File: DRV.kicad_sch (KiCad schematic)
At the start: 51 parts, among them J2 01x03_MotorTerminal, Q1 NE006NG, Q2 NE006NG, Q3 NE006NG, Q4 NE006NG, Q5 NE006NG, Q6 NE006NG, U7 DRV8353SRTAR

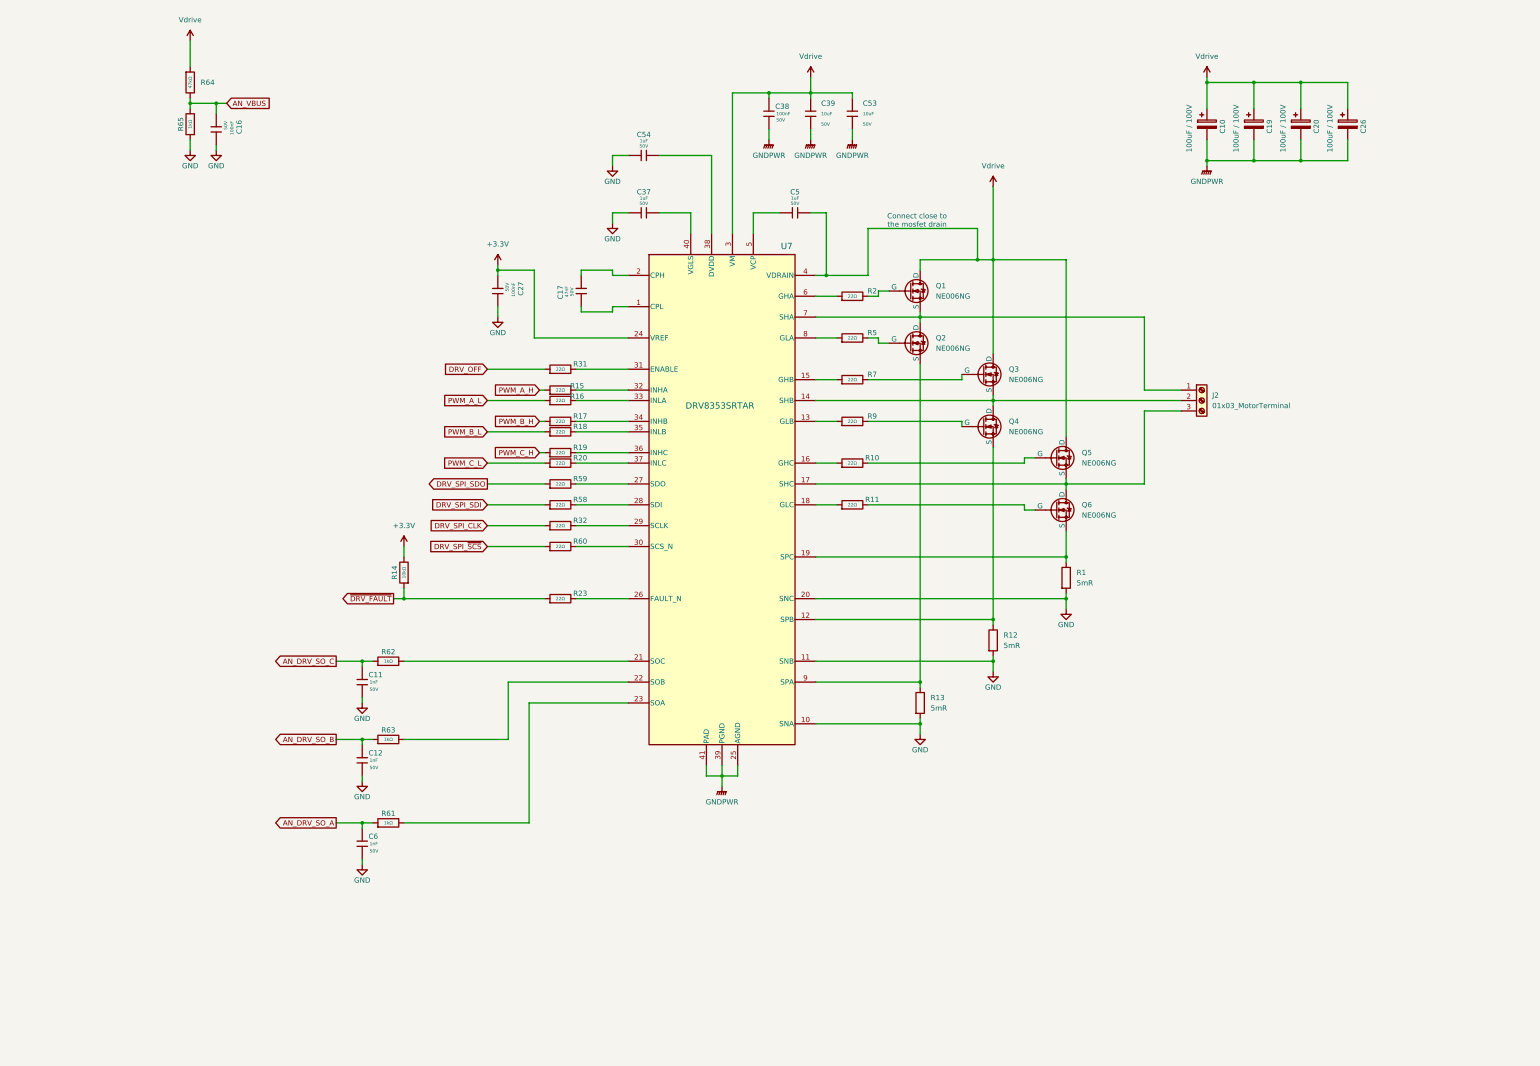
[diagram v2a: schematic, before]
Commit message: Circular pcb edge cut
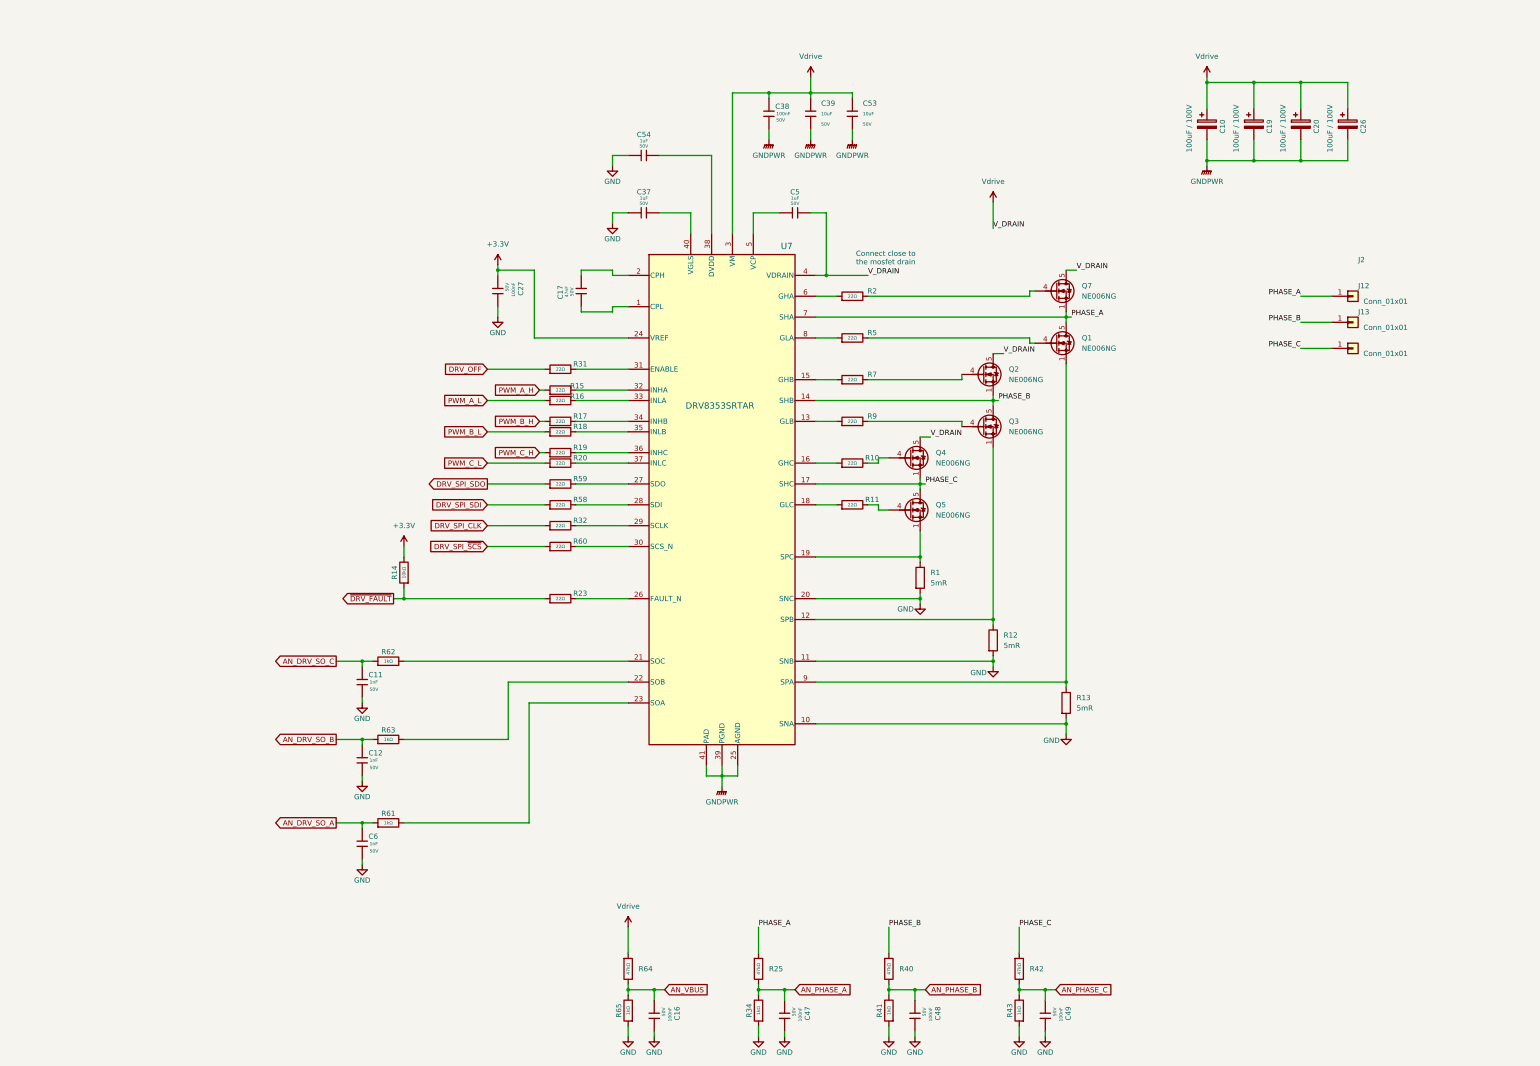
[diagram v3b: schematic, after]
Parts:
- removed J2: 01x03_MotorTerminal, Connector_Phoenix_MC:PhoenixContact_MC_1,5_3-G-3.5_1x03_P3.50mm_Horizontal, symbol Connector:Screw_Terminal_01x03
- removed Q1, Q2, Q3, Q4, Q5, Q6: NE006NG, Package_DFN_QFN:AO_DFN-8-1EP_5.55x5.2mm_P1.27mm_EP4.12x4.6mm, symbol Simulation_SPICE:NMOS
- added C47, C48, C49: 100nF, PCM_JLCPCB:C_0603, symbol PCM_JLCPCB-Capacitors:0603,100nF
- added J12, J13, J2: Conn_01x01, Connector_Wire:SolderWire-2.5sqmm_1x01_D2.4mm_OD3.6mm, symbol Connector_Generic:Conn_01x01
- added Q1, Q2, Q3, Q4, Q5, Q7: NE006NG, Package_DFN_QFN:AO_DFN-8-1EP_5.55x5.2mm_P1.27mm_EP4.12x4.6mm, symbol Transistor_FET:FDMS8350LET40
- added R25, R40, R42: 47kΩ, PCM_JLCPCB:R_0603, symbol PCM_JLCPCB-Resistors:0603,47kΩ
- added R34, R41, R43: 1kΩ, PCM_JLCPCB:R_0603, symbol PCM_JLCPCB-Resistors:0603,1kΩ
- U7: footprint RTA0040B -> footprints:RTA0040B
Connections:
- net GND: now also C47.2, C48.2, C49.2, R34.1, R41.1, R43.1
- net Vdrive: now also Q2.5 (D), Q4.5 (D), Q7.5 (D)
- net at R10.2: now also Q4.4 (G)
- net PHASE_C: now reaches U7.17 (SHC)
- net PHASE_C: now also J13.1 (Pin_1), Q4.1 (S), Q4.2 (S), Q4.3 (S), Q5.5 (D), R42.1
- net at R5.2: now also Q1.4 (G)
- net at R13.1, U7.9 (SPA): now also Q1.1 (S), Q1.2 (S), Q1.3 (S)
- net PHASE_A: now reaches U7.7 (SHA)
- net PHASE_A: now also J2.1 (Pin_1), Q1.5 (D), Q7.1 (S), Q7.2 (S), Q7.3 (S), R25.1
- net at R2.2: now also Q7.4 (G)
- net at R11.2: now also Q5.4 (G)
- net at R1.1, U7.19 (SPC): now also Q5.1 (S), Q5.2 (S), Q5.3 (S)
- net at R7.2: now also Q2.4 (G)
- net PHASE_B: now reaches U7.14 (SHB)
- net PHASE_B: now also J12.1 (Pin_1), Q2.1 (S), Q2.2 (S), Q2.3 (S), Q3.5 (D), R40.1
- net at R9.2: now also Q3.4 (G)
- net at R12.1, U7.12 (SPB): now also Q3.1 (S), Q3.2 (S), Q3.3 (S)
- new net AN_PHASE_A: C47.1, R25.2, R34.2
- new net AN_PHASE_B: C48.1, R40.2, R41.2
- new net AN_PHASE_C: C49.1, R42.2, R43.2
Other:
- moved on the sheet: C16, R1, R13, R64, R65

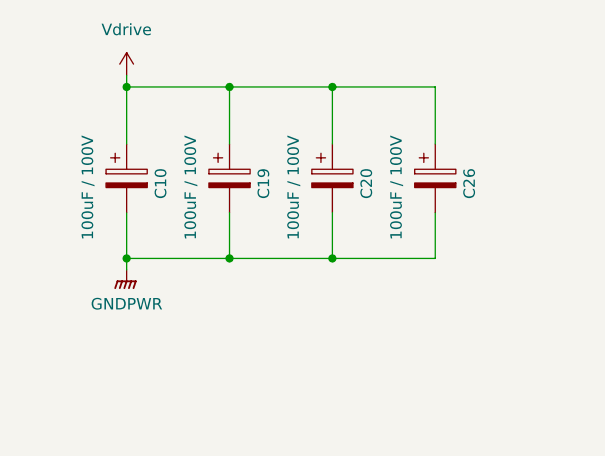
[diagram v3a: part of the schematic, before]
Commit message: Rough placement
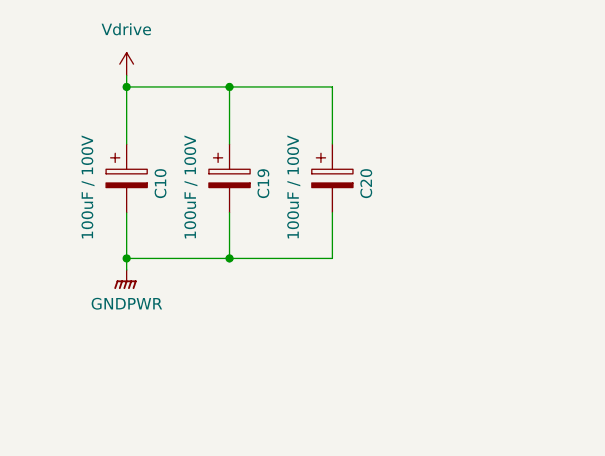
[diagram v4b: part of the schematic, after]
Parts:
- removed C26: 100uF / 100V, Capacitor_SMD:CP_Elec_10x10.5, symbol Device:C_Polarized
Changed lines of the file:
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@@
 	)
 	(junction
-		(at 332.74 57.15)
-		(diameter 0)
-		(color 0 0 0 0)
-	)
-	(junction
 		(at 275.59 184.15)
 		(diameter 0)
@@
 	)
 	(junction
-		(at 332.74 38.1)
-		(diameter 0)
-		(color 0 0 0 0)
-	)
-	(junction
 		(at 114.3 163.83)
 		(diameter 0)
@@
 	(wire
 		(pts
-			(xy 332.74 38.1) (xy 344.17 38.1)
-		)
-		(stroke
-			(width 0)
-			(type default)
-		)
-	)
-	(wire
-		(pts
 			(xy 214.63 95.25) (xy 275.59 95.25)
 		)
@@
 	(wire
 		(pts
-			(xy 344.17 57.15) (xy 344.17 52.07)
-		)
-		(stroke
-			(width 0)
-			(type default)
-		)
-	)
-	(wire
-		(pts
 			(xy 232.41 267.97) (xy 232.41 270.51)
 		)
@@
 	(wire
 		(pts
-			(xy 344.17 38.1) (xy 344.17 44.45)
-		)
-		(stroke
-			(width 0)
-			(type default)
-		)
-	)
-	(wire
-		(pts
 			(xy 257.81 127) (xy 257.81 168.91)
 		)
@@
 	(wire
 		(pts
-			(xy 332.74 57.15) (xy 344.17 57.15)
-		)
-		(stroke
-			(width 0)
-			(type default)
-		)
-	)
-	(wire
-		(pts
 			(xy 214.63 115.57) (xy 257.81 115.57)
 		)
@@
 					(unit 1)
 				)
-			)
-		)
-	)
-	(symbol
-		(lib_id "Device:C_Polarized")
-		(at 344.17 48.26 0)
-		(unit 1)
-		(exclude_from_sim no)
-		(in_bom yes)
-		(on_board yes)
-		(dnp no)
-		(property "Reference" "C26"
-			(at 347.98 50.546 90)
-			(effects
-				(font
-					(size 1.27 1.27)
-				)
-				(justify left)
-			)
-		)
-		(property "Value" "100uF / 100V"
-			(at 339.852 55.118 90)
-			(effects
-				(font
-					(size 1.27 1.27)
-				)
-				(justify left)
-			)
-		)
-		(property "Footprint" "Capacitor_SMD:CP_Elec_10x10.5"
-			(at 345.1352 52.07 0)
-			(effects
-				(font
-					(size 1.27 1.27)
-				)
-				(hide yes)
-			)
-		)
-		(property "Datasheet" "~"
-			(at 344.17 48.26 0)
-			(effects
-				(font
-					(size 1.27 1.27)
-				)
-				(hide yes)
-			)
-		)
-		(property "Description" "Polarized capacitor"
-			(at 344.17 48.26 0)
-			(effects
-				(font
-					(size 1.27 1.27)
-				)
-				(hide yes)
-			)
-		)
-		(property "LCSC" "C3008502"
-			(at 344.17 48.26 0)
-			(effects
-				(font
-					(size 1.27 1.27)
-				)
-				(hide yes)
-			)
-		)
-		(pin "2"
-		)
-		(pin "1"
-		)
-		(instances
-			(project "PiccoloMotorDriver"
-				(path "/cc8a13e7-b1a6-4cbd-adcd-4feb8b2e2369/7be09983-144f-4bac-af55-89c406995975"
-					(reference "C26")
-					(unit 1)
-				)

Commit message: Placement, some layout
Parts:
- removed C47, C48, C49: 100nF, PCM_JLCPCB:C_0603, symbol PCM_JLCPCB-Capacitors:0603,100nF
- removed R25, R40, R42: 47kΩ, PCM_JLCPCB:R_0603, symbol PCM_JLCPCB-Resistors:0603,47kΩ
- removed R34, R41, R43: 1kΩ, PCM_JLCPCB:R_0603, symbol PCM_JLCPCB-Resistors:0603,1kΩ
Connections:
- net ~{DRV_FAULT}: no longer R14.1
- net at R23.2, U7.26 (FAULT_N): now also R14.1
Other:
- moved on the sheet: J12, J13, J2, R23

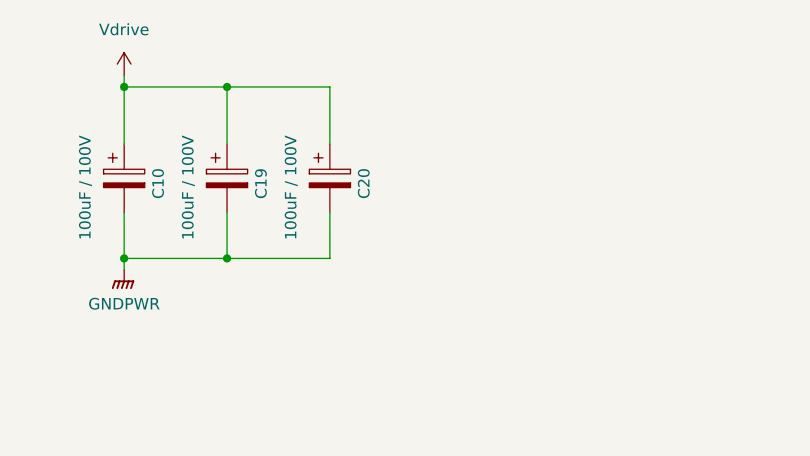
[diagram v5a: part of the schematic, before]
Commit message: Reduced number of 10uF caps
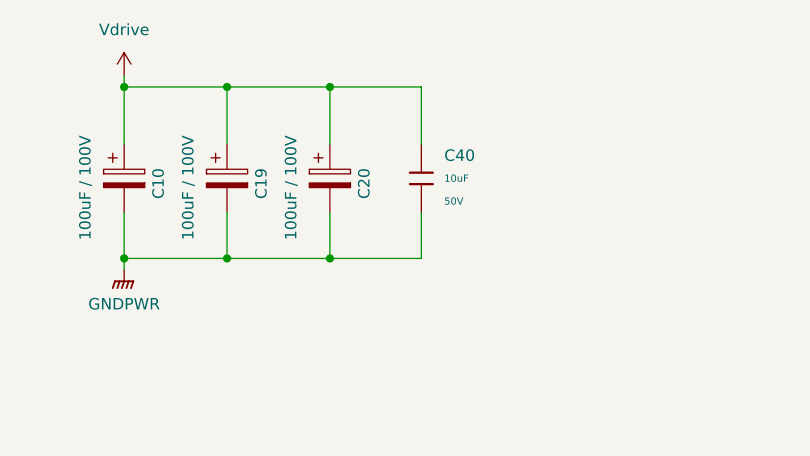
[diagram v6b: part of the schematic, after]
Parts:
- added C40: 10uF, PCM_JLCPCB:C_1206, symbol PCM_JLCPCB-Capacitors:1206,10uF
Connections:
- net GNDPWR: now also C40.2
- net Vdrive: now also C40.1

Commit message: DRC check - fine tuning
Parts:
- added R25: 10kΩ, PCM_JLCPCB:R_0603, symbol PCM_JLCPCB-Resistors:0603,10kΩ
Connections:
- net +3.3V: now also R25.2
- net at R59.2, U7.27 (SDO): now also R25.1
- net DRV_OFF renamed DRV_ENABLE
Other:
- moved on the sheet: J12, J13, J2, R59

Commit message: Drc, Bom done
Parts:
- U7: LCSC (none) -> C701785
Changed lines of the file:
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@@
+			)
+		)
+		(property "LCSC" "C701785"
+			(at 207.518 77.978 0)
+			(effects
+				(font
+					(size 1.27 1.27)
+				)
+				(hide yes)
 			)
 		)
